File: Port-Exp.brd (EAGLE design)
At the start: 97.5 x 22.9 mm, 29 parts, among them IC1 MEGA8-P, IC2 317EMP, U1 MAX4762EUB, U2 MAX40077AUA+21-0036K-M

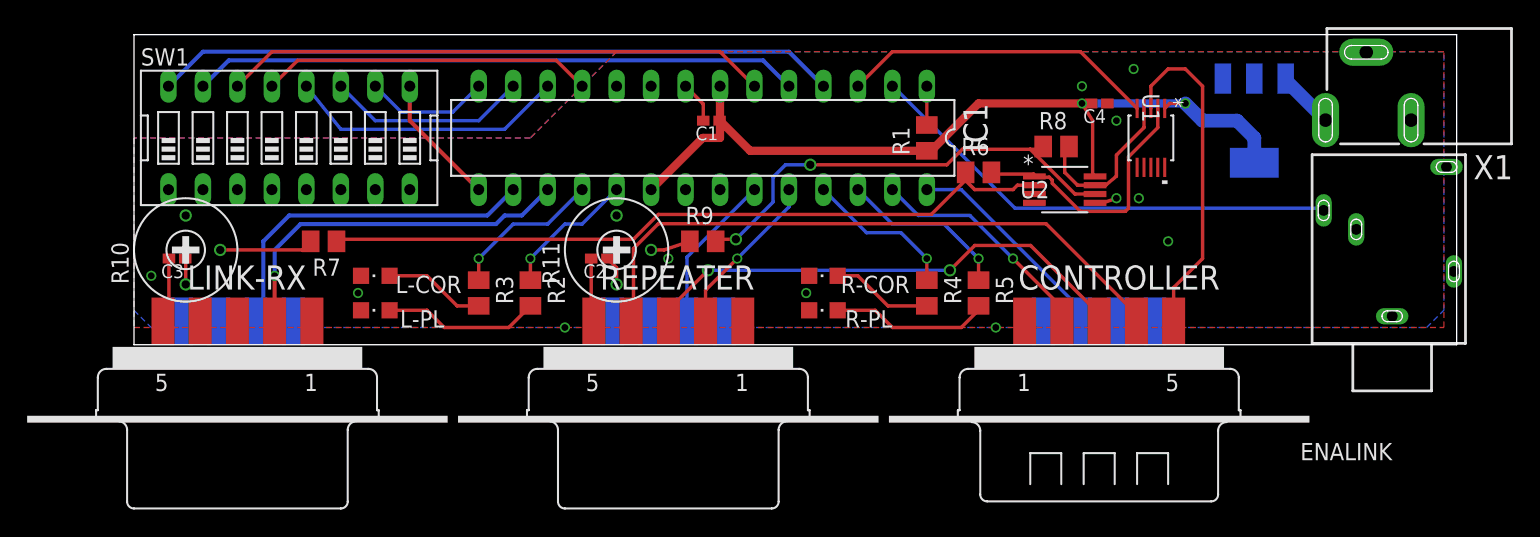
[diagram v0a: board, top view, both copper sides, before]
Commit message: tweaked sizes, added label to board, adjusted schematic to print on one sheet
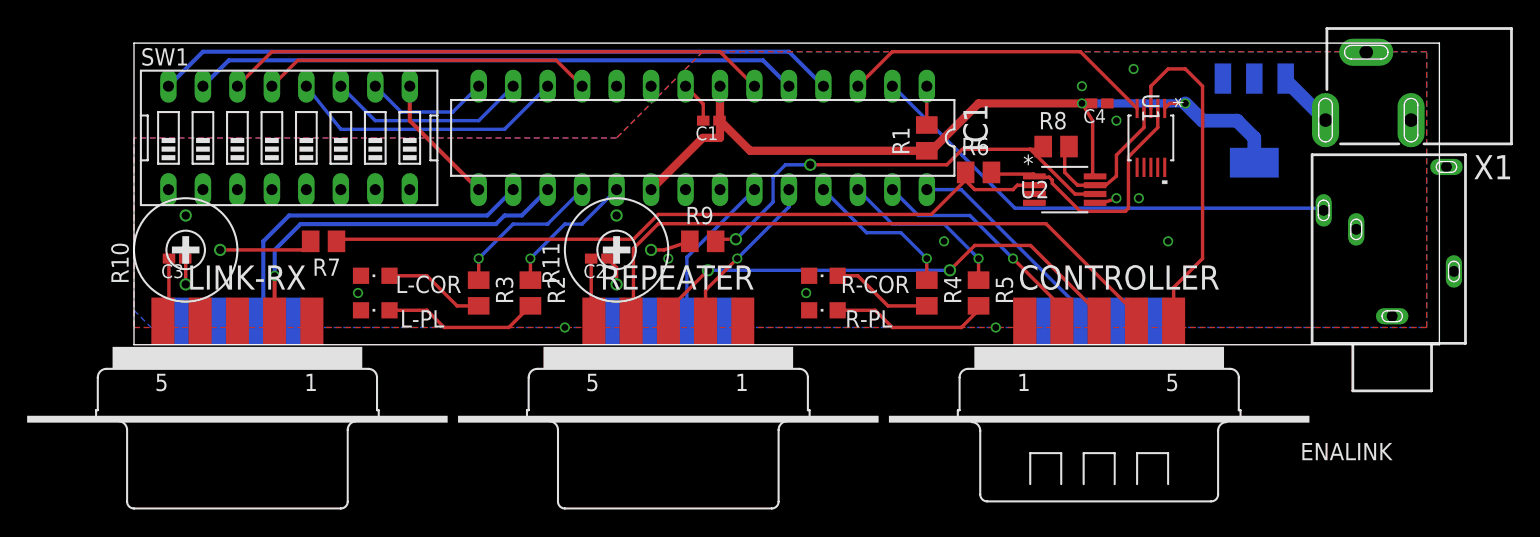
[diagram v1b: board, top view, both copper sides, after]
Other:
- board size 97.5 x 22.9 mm -> 96.2 x 22.2 mm
- board text added: "CONTROLLER"
- board text added: "LINK"
- board text added: "Made for TMRA"
- board text added: "RPT"
- board text added: "https://github.com/kc8ufv/Club-Port-Expander"
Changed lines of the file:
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@@
 <board>
 <plain>
-<wire x1="0" y1="0" x2="97.46" y2="0" width="0" layer="20"/>
-<wire x1="97.46" y1="0" x2="97.46" y2="22.85" width="0" layer="20"/>
-<wire x1="97.46" y1="22.85" x2="0" y2="22.85" width="0" layer="20"/>
-<wire x1="0" y1="22.85" x2="0" y2="0" width="0" layer="20"/>
+<wire x1="0" y1="0" x2="96.19" y2="0" width="0" layer="20"/>
+<wire x1="96.19" y1="0" x2="96.19" y2="22.225" width="0" layer="20"/>
+<wire x1="96.19" y1="22.225" x2="0" y2="22.225" width="0" layer="20"/>
+<wire x1="0" y1="22.225" x2="0" y2="0" width="0" layer="20"/>
+<text x="63.5" y="15.24" size="1.27" layer="26" font="fixed" rot="MR0">https://github.com/kc8ufv/Club-Port-Expander</text>
+<text x="80.01" y="3.81" size="1.778" layer="26" rot="MR0">CONTROLLER</text>
+<text x="45.72" y="0" size="1.778" layer="26" rot="MR0">CONTROLLER</text>
+<text x="40.64" y="3.81" size="1.778" layer="26" rot="MR0">RPT</text>
+<text x="10.16" y="3.81" size="1.778" layer="26" rot="MR0">LINK</text>
+<text x="48.26" y="12.7" size="1.27" layer="26" font="fixed" rot="MR0">Made for TMRA</text>
 </plain>
 <attributes>
@@
 <via x="16.51" y="3.81" extent="1-16" drill="0.5"/>
 <via x="49.53" y="3.81" extent="1-16" drill="0.5"/>
-<via x="1.27" y="5.08" extent="1-16" drill="0.5"/>
 <via x="31.75" y="1.27" extent="1-16" drill="0.5"/>
 <via x="63.5" y="1.27" extent="1-16" drill="0.5"/>
@@
 <polygon width="0.254" layer="1">
 <vertex x="0" y="1.27"/>
-<vertex x="96.52" y="1.27"/>
-<vertex x="96.52" y="21.59"/>
-<vertex x="35.56" y="21.59"/>
-<vertex x="29.21" y="15.24"/>
+<vertex x="95.25" y="1.27"/>
+<vertex x="95.25" y="21.59"/>
+<vertex x="41.91" y="21.59"/>
+<vertex x="35.56" y="15.24"/>
 <vertex x="0" y="15.24"/>
 </polygon>
 <polygon width="0.254" layer="16">
-<vertex x="96.52" y="21.59"/>
-<vertex x="35.56" y="21.59"/>
-<vertex x="29.21" y="15.24"/>
+<vertex x="95.25" y="21.59"/>
+<vertex x="41.91" y="21.59"/>
+<vertex x="35.56" y="15.24"/>
 <vertex x="0" y="15.24"/>
 <vertex x="0" y="2.54"/>
 <vertex x="1.27" y="1.27"/>
 <vertex x="95.25" y="1.27"/>
-<vertex x="96.52" y="2.54"/>
 </polygon>
 <via x="39.37" y="6.35" extent="1-16" drill="0.5"/>
 <via x="73.66" y="20.32" extent="1-16" drill="0.5"/>
+<via x="59.69" y="7.62" extent="1-16" drill="0.5"/>
 </signal>
 <signal name="N$4">
